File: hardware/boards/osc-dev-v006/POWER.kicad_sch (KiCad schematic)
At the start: 17 parts, among them J1 JST-PH-H, J2 TERM, U1 HT7533-1

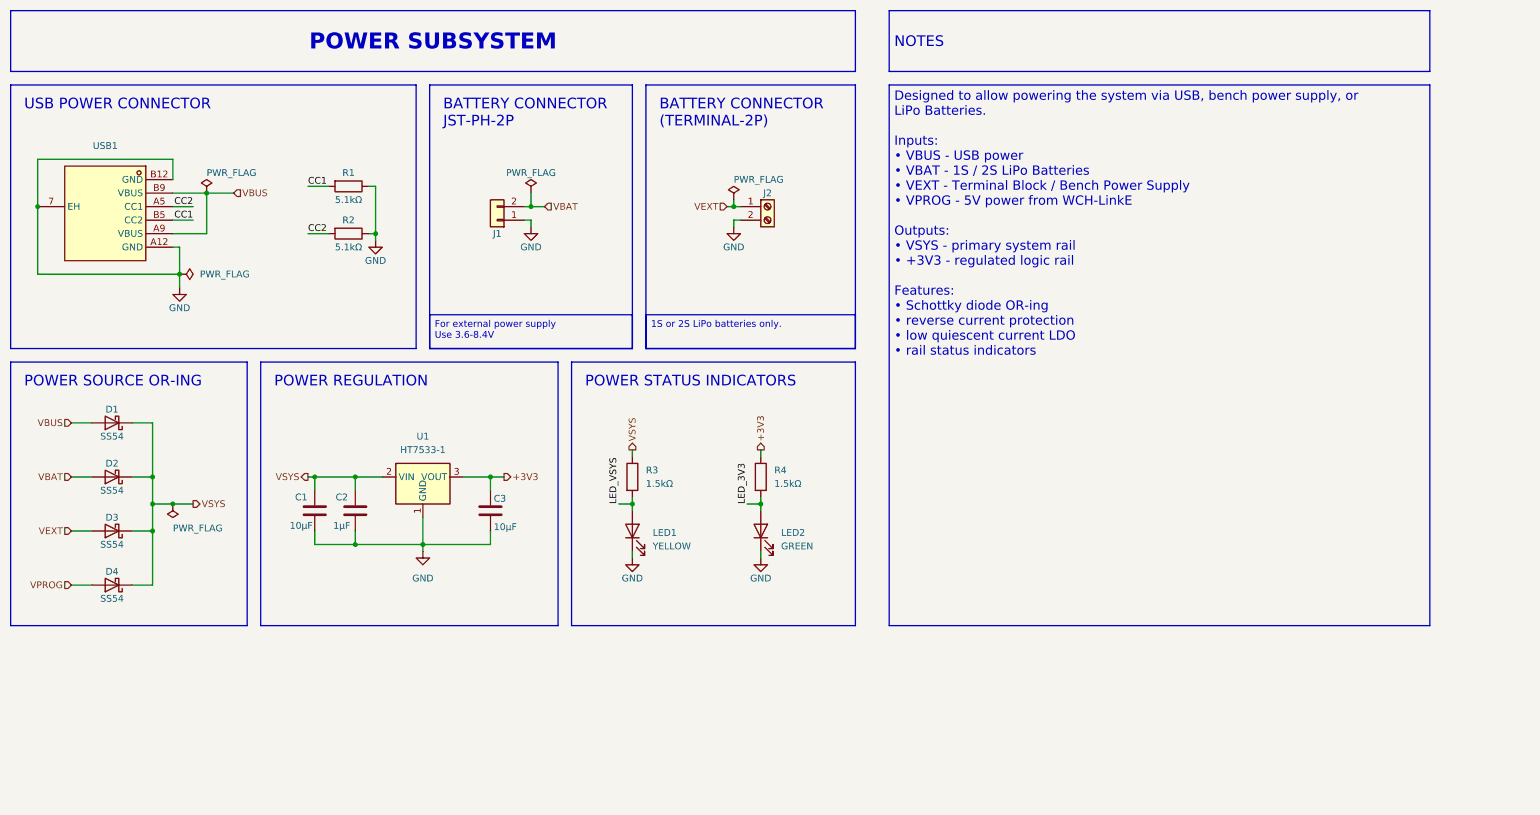
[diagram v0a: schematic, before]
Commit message: hw: osc-dev-v006 rev-2a - 6l precision respin, direct-wire bus, docs
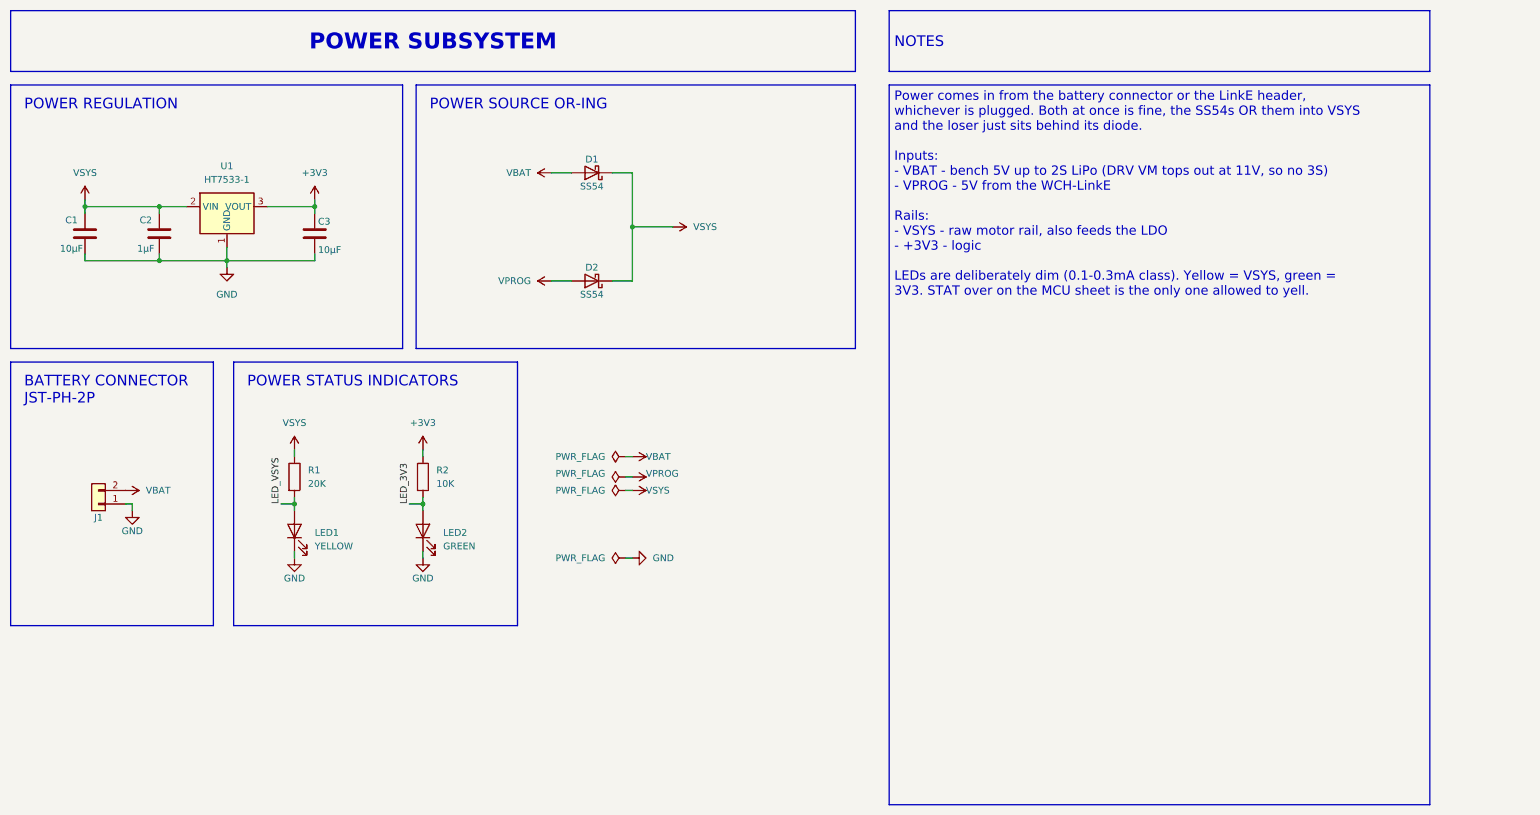
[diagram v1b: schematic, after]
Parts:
- removed D1, D3: SS54, Diode_SMD:D_SMA_Handsoldering, symbol Diode:SS34
- removed J2: TERM, shared:CONN-TH_2P-P5.00_WJ500V-5.08-2P, symbol Connector:Screw_Terminal_01x02
- removed R1, R2: 5.1kΩ, Resistor_SMD:R_0805_2012Metric_Pad1.20x1.40mm_HandSolder, symbol Device:R
- removed USB1: TYPE-C-H, shared:TYPE-C-SMD_TYPE-C-6P-073, symbol shared:TYPE-C6P(073)
- C1, C3: LCSC C440198 -> C15850; MFPN GRM21BR61H106KE43L -> CL21A106KAYNNNE
- C2: footprint Capacitor_SMD:C_0805_2012Metric_Pad1.18x1.45mm_HandSolder -> Capacitor_SMD:C_0603_1608Metric_Pad1.08x0.95mm_HandSolder; LCSC C28323 -> C29936
- LED1: footprint LED_SMD:LED_0805_2012Metric -> LED_SMD:LED_0603_1608Metric_Pad1.05x0.95mm_HandSolder; LCSC C2296 -> C51933295
- LED2: footprint LED_SMD:LED_0805_2012Metric -> LED_SMD:LED_0603_1608Metric_Pad1.05x0.95mm_HandSolder; LCSC C2297 -> C51933293
- R1: renamed from R3; value 1.5kΩ -> 20K; footprint Resistor_SMD:R_0805_2012Metric_Pad1.20x1.40mm_HandSolder -> Resistor_SMD:R_0603_1608Metric_Pad0.98x0.95mm_HandSolder; LCSC C4310 -> C2907011; MFPN 0805W8F1501T5E -> FRC0805F2002TS
- R2: renamed from R4; value 1.5kΩ -> 10K; footprint Resistor_SMD:R_0805_2012Metric_Pad1.20x1.40mm_HandSolder -> Resistor_SMD:R_0603_1608Metric_Pad0.98x0.95mm_HandSolder; LCSC C4310 -> C2906982; MFPN 0805W8F1501T5E -> FRC0805F1002TS
- renumbered D2 to D1, D4 to D2
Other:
- note removed: "BATTERY CONNECTOR (TERMINAL-2P)"
- note removed: "USB POWER CONNECTOR"
- title: POWER -> ${PROJECT} / ${BOARD}
- moved on the sheet: C1, C2, C3, D1, D2, J1, LED1, LED2, R1, R2, U1

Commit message: hw: v006 lcsc fields track rev-2a order substitutions
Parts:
- C2: LCSC C29936 -> C559769; MFPN CL21B105KBFNNNE -> CC0603KRX7R9BB105
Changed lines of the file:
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@@
 			)
 		)
-		(property "Datasheet" "https://www.lcsc.com/product-detail/C29936.html"
+		(property "Datasheet" "https://www.lcsc.com/product-detail/C559769.html"
 			(at 17.24 21.76 0)
 			(hide yes)
@@
 			)
 		)
-		(property "Description" "Unpolarized capacitor"
+		(property "Description" "1µF ±10% 50V X7R 0603"
 			(at 17.24 21.76 0)
 			(hide yes)
@@
 			)
 		)
-		(property "LCSC" "C29936"
+		(property "LCSC" "C559769"
 			(at 40.64 53.34 0)
 			(hide yes)
@@
 			)
 		)
-		(property "MFPN" "CL21B105KBFNNNE"
+		(property "MFPN" "CC0603KRX7R9BB105"
 			(at 40.64 53.34 0)
 			(hide yes)

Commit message: board: osc-dev-v006 rev 2a (#107)
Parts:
- Cp1: renamed from C1; value 10µF -> 10uF
- Cp2: renamed from C2; value 1µF -> 1uF
- Cp3: renamed from C3; value 10µF -> 10uF
- Dl1: renamed from LED1; JLC Type Standard -> (none); LCSC C51933295 -> C497929; MFPN KT-0805Y -> HL-PST-1608U32YC
- Dl2: renamed from LED2; JLC Type Standard -> (none); LCSC C51933293 -> C497927; MFPN KT-0805G -> HL-PST-1608U51GC
- Dp1: renamed from D1; JLC Type Basic -> (none)
- Dp2: renamed from D2; JLC Type Basic -> (none)
- J1: JLC Type Extended -> (none)
- Rl1: renamed from R1; MFPN FRC0805F2002TS -> FRC0603F2002TS
- Rl2: renamed from R2; MFPN FRC0805F1002TS -> FRC0603F1002TS
- U1: JLC Type Basic -> (none)
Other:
- note added: "3V3 LDO"
- note added: "Battery input JST-PH 2P"
- note added: "Rail indicators"
- note added: "Source OR-ing"
- note removed: "BATTERY CONNECTOR JST-PH-2P"
- note removed: "POWER REGULATION"
- note removed: "POWER SOURCE OR-ING"
- note removed: "POWER STATUS INDICATORS"
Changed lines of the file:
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@@
 		)
 	)
-	(text "BATTERY CONNECTOR\nJST-PH-2P"
+	(text "Battery input\nJST-PH 2P"
 		(exclude_from_sim no)
 		(at 17.78 82.55 0)
@@
 		)
 	)
-	(text "POWER REGULATION"
+	(text "3V3 LDO"
 		(exclude_from_sim no)
 		(at 17.78 30.48 0)
@@
 		)
 	)
-	(text "POWER STATUS INDICATORS"
+	(text "Rail indicators"
 		(exclude_from_sim no)
 		(at 59.69 82.55 0)
@@
 		)
 	)
-	(text "POWER SOURCE OR-ING"
+	(text "Source OR-ing"
 		(exclude_from_sim no)
 		(at 93.98 30.48 0)
@@
 		)
 	)
-	(text_box "Power comes in from the battery connector or the LinkE header, whichever is plugged. Both at once is fine, the SS54s OR them into VSYS and the loser just sits behind its diode.\n\nInputs:\n- VBAT - bench 5V up to 2S LiPo (DRV VM tops out at 11V, so no 3S)\n- VPROG - 5V from the WCH-LinkE\n\nRails:\n- VSYS - raw motor rail, also feeds the LDO\n- +3V3 - logic\n\nLEDs are deliberately dim (0.1-0.3mA class). Yellow = VSYS, green = 3V3. STAT over on the MCU sheet is the only one allowed to yell."
+	(text_box "Power comes in from the battery connector or the LinkE header, whichever is plugged. Both at once is fine, the SS54s OR them into VSYS and the loser just sits behind its diode.\n\nInputs:\n- VBAT - bench 5V up to 2S LiPo (DRV VM tops out at 11V, so no 3S)\n- VPROG - 5V from the WCH-LinkE\n\nRails:\n- VSYS - raw motor rail, also feeds the LDO\n- +3V3 - logic, and the DRV8212P VCC. One rail, no separate driver rail.\n\nLEDs are deliberately dim (0.1-0.3mA class). Yellow = VSYS, green = 3V3. STAT over on the MCU sheet is the only firmware-driven one."
 		(exclude_from_sim no)
 		(at 180.34 27.94 0)
@@
 		(in_pos_files yes)
 		(dnp no)
-		(property "Reference" "C2"
+		(property "Reference" "Cp2"
 			(at 40.64 53.34 0)
 			(show_name no)
@@
 			)
 		)
-		(property "Value" "1µF"
+		(property "Value" "1uF"
 			(at 40.64 58.674 0)
 			(show_name no)
@@
 			)
 		)
-		(property "Description" "1µF ±10% 50V X7R 0603"
+		(property "Description" "1µF +/-10% 50V X7R 0603"
 			(at 17.24 21.76 0)
 			(hide yes)
@@
 			(project "osc-dev-v006"
 				(path "/6062e7d2-0c72-467e-b49c-6387ba053e09/1e728d76-963a-4d02-a5f6-92f3889aa8bb"
-					(reference "C2")
+					(reference "Cp2")
 					(unit 1)
 				)
@@
 		(dnp no)
 		(fields_autoplaced yes)
-		(property "Reference" "LED1"
+		(property "Reference" "Dl1"
 			(at 72.39 112.0774 90)
 			(show_name no)
@@
 			)
 		)
-		(property "Datasheet" "https://www.lcsc.com/product-detail/C51933295.html"
+		(property "Datasheet" "https://www.lcsc.com/product-detail/C497929.html"
 			(at 68.58 111.76 0)
 			(hide yes)
@@
 			)
 		)
-		(property "LCSC" "C51933295"
+		(property "LCSC" "C497929"
 			(at 72.39 112.0774 0)
 			(hide yes)
@@
 			)
 		)
-		(property "MFPN" "KT-0805Y"
+		(property "MFPN" "HL-PST-1608U32YC"
 			(at 72.39 112.0774 0)
 			(hide yes)
@@
 			)
 		)
-		(property "Sim.Pins" "1=K 2=A"
-			(at 68.58 111.76 0)
-			(hide yes)
-			(show_name no)
-			(do_not_autoplace no)
-			(effects
-				(font
-					(size 1.27 1.27)
-				)
-			)
-		)
-		(property "JLC Type" "Standard"
-			(at 68.58 111.76 90)
-			(hide yes)
-			(show_name no)
-			(do_not_autoplace no)
-			(effects
-				(font
-					(size 1.27 1.27)
-				)
-			)
-		)
 		(pin "2"
 		)
@@
 			(project "osc-dev-v006"
 				(path "/6062e7d2-0c72-467e-b49c-6387ba053e09/1e728d76-963a-4d02-a5f6-92f3889aa8bb"
-					(reference "LED1")
+					(reference "Dl1")
 					(unit 1)
 				)
@@
 		(dnp no)
 		(fields_autoplaced yes)
-		(property "Reference" "R1"
+		(property "Reference" "Rl1"
 			(at 71.12 100.3299 0)
 			(show_name no)
@@
 			)
 		)
-		(property "MFPN" "FRC0805F2002TS"
+		(property "MFPN" "FRC0603F2002TS"
 			(at 71.12 100.3299 0)
 			(hide yes)
@@
 			(project "osc-dev-v006"
 				(path "/6062e7d2-0c72-467e-b49c-6387ba053e09/1e728d76-963a-4d02-a5f6-92f3889aa8bb"
-					(reference "R1")
+					(reference "Rl1")
 					(unit 1)
 				)
@@
 			)
 		)
-		(property "JLC Type" "Basic"
-			(at 55.88 53.34 0)
-			(hide yes)
-			(show_name no)
-			(do_not_autoplace no)
-			(effects
-				(font
-					(size 1.27 1.27)
-				)
-			)
-		)
 		(pin "2"
 		)
@@
 			)
 		)
-		(property "JLC Type" "Extended"
-			(at 31.75 106.68 0)
-			(hide yes)
-			(show_name no)
-			(do_not_autoplace no)
-			(effects
-				(font
-					(size 1.27 1.27)
-				)
-			)
-		)
 		(pin "1"
 		)
@@
 		(in_pos_files yes)
 		(dnp no)
-		(property "Reference" "D2"
+		(property "Reference" "Dp2"
 			(at 124.46 62.23 0)
 			(show_name no)
@@
 			)
 		)
-		(property "JLC Type" "Basic"
-			(at 124.46 64.77 0)
-			(hide yes)
-			(show_name no)
-			(do_not_autoplace no)
-			(effects
-				(font
-					(size 1.27 1.27)
-				)
-			)
-		)
 		(pin "1"
 		)
@@
 			(project "osc-dev-v006"
 				(path "/6062e7d2-0c72-467e-b49c-6387ba053e09/1e728d76-963a-4d02-a5f6-92f3889aa8bb"
-					(reference "D2")
+					(reference "Dp2")
 					(unit 1)
 				)
@@
 		(in_pos_files yes)
 		(dnp no)
-		(property "Reference" "D1"
+		(property "Reference" "Dp1"
 			(at 124.46 41.91 0)
 			(show_name no)
@@
 			)
 		)
-		(property "JLC Type" "Basic"
-			(at 124.46 44.45 0)
-			(hide yes)
-			(show_name no)
-			(do_not_autoplace no)
-			(effects
-				(font
-					(size 1.27 1.27)
-				)
-			)
-		)
 		(pin "1"
 		)
@@
 			(project "osc-dev-v006"
 				(path "/6062e7d2-0c72-467e-b49c-6387ba053e09/1e728d76-963a-4d02-a5f6-92f3889aa8bb"
-					(reference "D1")
+					(reference "Dp1")
 					(unit 1)
 				)
@@
 		(in_pos_files yes)
 		(dnp no)
-		(property "Reference" "C1"
+		(property "Reference" "Cp1"
 			(at 26.67 53.34 0)
 			(show_name no)
@@
 			)
 		)
-		(property "Value" "10µF"
+		(property "Value" "10uF"
 			(at 26.67 58.674 0)
 			(show_name no)
@@
 			(project "osc-dev-v006"
 				(path "/6062e7d2-0c72-467e-b49c-6387ba053e09/1e728d76-963a-4d02-a5f6-92f3889aa8bb"
-					(reference "C1")
+					(reference "Cp1")
 					(unit 1)
 				)
@@
 		(in_pos_files yes)
 		(dnp no)
-		(property "Reference" "C3"
+		(property "Reference" "Cp3"
 			(at 74.168 53.594 0)
 			(show_name no)
@@
 			)
 		)
-		(property "Value" "10µF"
+		(property "Value" "10uF"
 			(at 75.184 58.928 0)
 			(show_name no)
@@
 			(project "osc-dev-v006"
 				(path "/6062e7d2-0c72-467e-b49c-6387ba053e09/1e728d76-963a-4d02-a5f6-92f3889aa8bb"
-					(reference "C3")
+					(reference "Cp3")
 					(unit 1)
 				)
@@
 		(dnp no)
 		(fields_autoplaced yes)
-		(property "Reference" "LED2"
+		(property "Reference" "Dl2"
 			(at 96.52 112.0774 90)
 			(show_name no)
@@
 			)
 		)
-		(property "Datasheet" "https://www.lcsc.com/product-detail/C51933293.html"
+		(property "Datasheet" "https://www.lcsc.com/product-detail/C497927.html"
 			(at 92.71 111.76 0)
 			(hide yes)
@@
 			)
 		)
-		(property "LCSC" "C51933293"
+		(property "LCSC" "C497927"
 			(at 96.52 112.0774 0)
 			(hide yes)
@@
 			)
 		)
-		(property "MFPN" "KT-0805G"
+		(property "MFPN" "HL-PST-1608U51GC"
 			(at 96.52 112.0774 0)
 			(hide yes)
@@
 			)
 		)
-		(property "Sim.Pins" "1=K 2=A"
-			(at 92.71 111.76 0)
-			(hide yes)
-			(show_name no)
-			(do_not_autoplace no)
-			(effects
-				(font
-					(size 1.27 1.27)
-				)
-			)
-		)
-		(property "JLC Type" "Standard"
-			(at 92.71 111.76 90)
-			(hide yes)
-			(show_name no)
-			(do_not_autoplace no)
-			(effects
-				(font
-					(size 1.27 1.27)
-				)
-			)
-		)
 		(pin "2"
 		)
@@
 			(project "osc-dev-v006"
 				(path "/6062e7d2-0c72-467e-b49c-6387ba053e09/1e728d76-963a-4d02-a5f6-92f3889aa8bb"
-					(reference "LED2")
+					(reference "Dl2")
 					(unit 1)
 				)
@@
 		(dnp no)
 		(fields_autoplaced yes)
-		(property "Reference" "R2"
+		(property "Reference" "Rl2"
 			(at 95.25 100.3299 0)
 			(show_name no)
@@
 			)
 		)
-		(property "MFPN" "FRC0805F1002TS"
+		(property "MFPN" "FRC0603F1002TS"
 			(at 95.25 100.3299 0)
 			(hide yes)
@@
 			(project "osc-dev-v006"
 				(path "/6062e7d2-0c72-467e-b49c-6387ba053e09/1e728d76-963a-4d02-a5f6-92f3889aa8bb"
-					(reference "R2")
+					(reference "Rl2")
 					(unit 1)
 				)
